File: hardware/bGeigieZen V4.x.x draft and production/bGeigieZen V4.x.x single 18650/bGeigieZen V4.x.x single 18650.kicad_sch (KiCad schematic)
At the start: 8 parts, among them J1 M5 2x15 pin, J2 Geiger IRover, J3 GPS, J4 Geiger Safepulse, J5 Extra support header

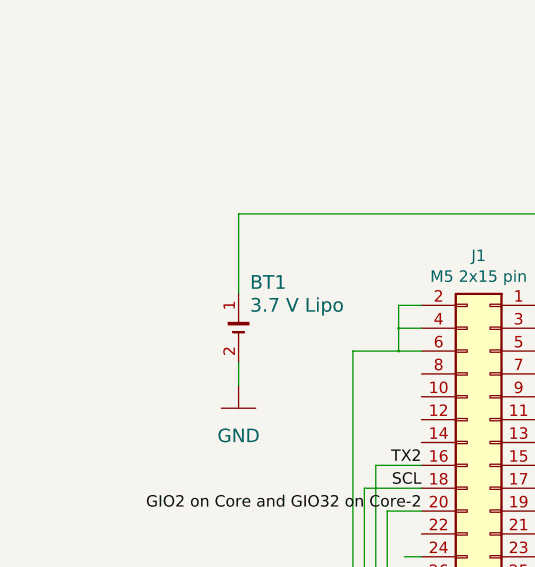
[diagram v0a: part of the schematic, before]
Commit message: reverses axp192 power setup (mistake)
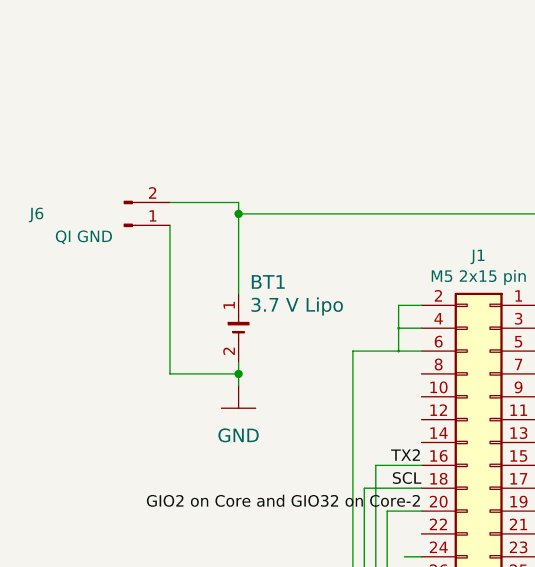
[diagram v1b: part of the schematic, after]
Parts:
- added J6: QI GND, Connector_JST:JST_PH_B2B-PH-K_1x02_P2.00mm_Vertical, symbol Connector:Conn_01x02_Male
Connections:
- net BAT: now also J6.2 (Pin_2)
- net GND: now also J6.1 (Pin_1)
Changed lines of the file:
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@@
+	)
+	(junction
+		(at 113.03 83.82)
+		(diameter 0)
+		(color 0 0 0 0)
 	)
 	(junction
@@
 	)
 	(junction
+		(at 113.03 66.04)
+		(diameter 0)
+		(color 0 0 0 0)
+	)
+	(junction
 		(at 187.96 68.58)
 		(diameter 0.3048)
@@
 	(wire
 		(pts
+			(xy 105.41 67.31) (xy 105.41 83.82)
+		)
+		(stroke
+			(width 0)
+			(type default)
+		)
+	)
+	(wire
+		(pts
 			(xy 113.03 66.04) (xy 151.765 66.04)
 		)
@@
 	(wire
 		(pts
+			(xy 105.41 83.82) (xy 113.03 83.82)
+		)
+		(stroke
+			(width 0)
+			(type default)
+		)
+	)
+	(wire
+		(pts
 			(xy 187.96 53.975) (xy 187.96 68.58)
 		)
@@
 	(wire
 		(pts
+			(xy 113.03 64.77) (xy 113.03 66.04)
+		)
+		(stroke
+			(width 0)
+			(type default)
+		)
+	)
+	(wire
+		(pts
+			(xy 113.03 83.82) (xy 113.03 85.09)
+		)
+		(stroke
+			(width 0)
+			(type default)
+		)
+	)
+	(wire
+		(pts
 			(xy 172.72 82.55) (xy 172.72 125.73)
 		)
@@
 	(wire
 		(pts
-			(xy 113.03 82.55) (xy 113.03 85.09)
+			(xy 113.03 82.55) (xy 113.03 83.82)
 		)
 		(stroke
@@
 			(width 0)
 			(type solid)
+		)
+	)
+	(wire
+		(pts
+			(xy 105.41 64.77) (xy 113.03 64.77)
+		)
+		(stroke
+			(width 0)
+			(type default)
 		)
 	)
@@
 					(unit 1)
 				)
+			)
+		)
+	)
+	(symbol
+		(lib_id "Connector:Conn_01x02_Male")
+		(at 100.33 67.31 0)
+		(mirror x)
+		(unit 1)
+		(exclude_from_sim no)
+		(in_bom yes)
+		(on_board yes)
+		(dnp no)
+		(property "Reference" "J6"
+			(at 91.44 66.04 0)
+			(effects
+				(font
+					(size 1.27 1.27)
+				)
+				(justify right)
+			)
+		)
+		(property "Value" "QI GND"
+			(at 99.06 68.58 0)
+			(effects
+				(font
+					(size 1.27 1.27)
+				)
+				(justify right)
+			)
+		)
+		(property "Footprint" "Connector_JST:JST_PH_B2B-PH-K_1x02_P2.00mm_Vertical"
+			(at 100.33 67.31 0)
+			(effects
+				(font
+					(size 1.27 1.27)
+				)
+				(hide yes)
+			)
+		)
+		(property "Datasheet" "~"
+			(at 100.33 67.31 0)
+			(effects
+				(font
+					(size 1.27 1.27)
+				)
+				(hide yes)
+			)
+		)
+		(property "Description" ""
+			(at 100.33 67.31 0)
+			(effects
+				(font
+					(size 1.27 1.27)
+				)
+				(hide yes)
+			)
+		)
+		(pin "1"
+		)
+		(pin "2"
+		)
+		(instances
+			(project "bGeigieZen V4.x.x single 18650"
+				(path "/c2e3a215-6a49-419d-95d1-595f35b17280"
+					(reference "J6")
+					(unit 1)
+				)

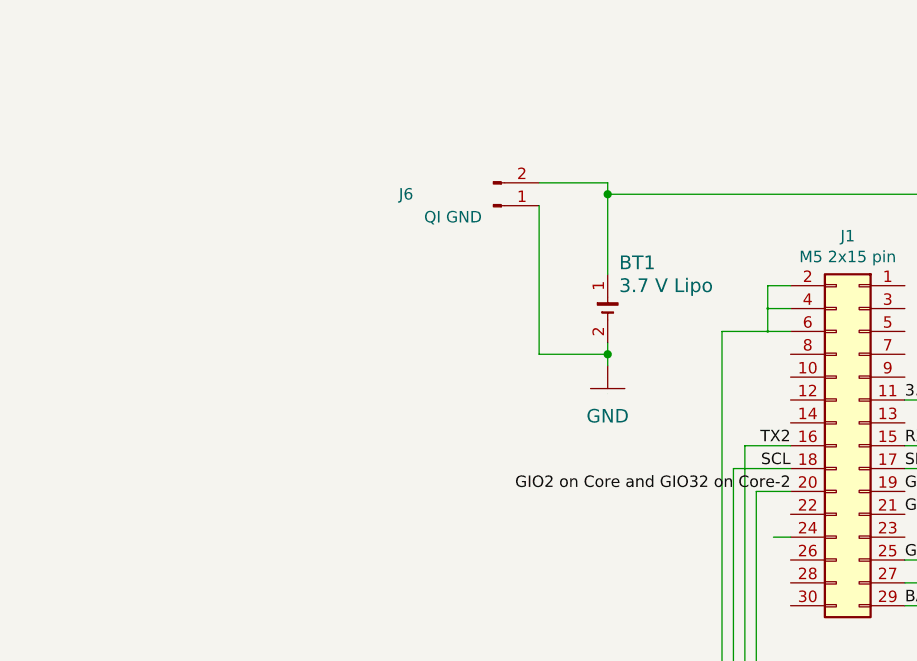
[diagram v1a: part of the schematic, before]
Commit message: Added grid and V4.0.5 boards
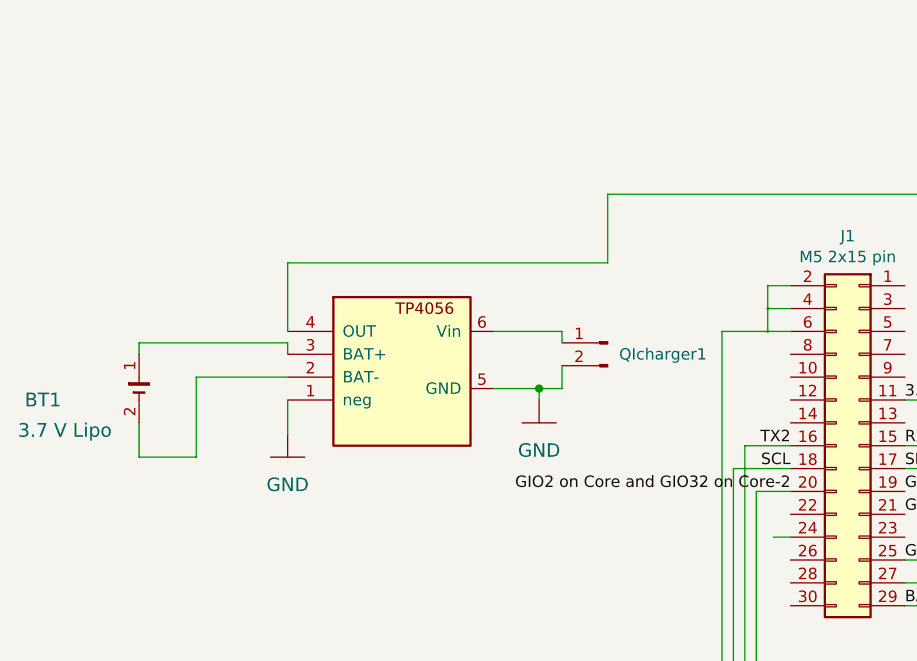
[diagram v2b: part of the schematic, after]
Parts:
- added TP4056: TP4056, bGeigieZen:TP4056, symbol tp4057:4057
- renumbered J6 to QIcharger1
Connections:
- net BAT: now also TP4056.4 (OUT); no longer BT1.1 (+), QIcharger1.2 (Pin_2)
- net GND: now also QIcharger1.2 (Pin_2), TP4056.1 (neg), TP4056.5 (GND); no longer BT1.2 (-), QIcharger1.1 (Pin_1)
- new net: BT1.1 (+), TP4056.3 (BAT+)
- new net: BT1.2 (-), TP4056.2 (BAT-)
- new net: QIcharger1.1 (Pin_1), TP4056.6 (Vin)
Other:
- moved on the sheet: BT1, QIcharger1

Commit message: Modified V4.0.5 board graphics
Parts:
- added SW1: SW_SPDT, bGeigieRaku_M5_1015:EG1206, symbol Switch:SW_SPDT
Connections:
- net BAT: now also SW1.1 (A); no longer TP4056.4 (OUT)
- new net: SW1.2 (B), TP4056.4 (OUT)
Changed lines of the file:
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@@
 	(wire
 		(pts
-			(xy 113.03 66.04) (xy 151.765 66.04)
+			(xy 113.03 66.04) (xy 115.57 66.04)
 		)
 		(stroke
@@
 	(wire
 		(pts
-			(xy 151.765 66.04) (xy 151.765 111.76)
-		)
-		(stroke
-			(width 0)
-			(type solid)
-		)
-	)
-	(wire
-		(pts
 			(xy 130.81 76.2) (xy 133.35 76.2)
 		)
@@
 	(wire
 		(pts
+			(xy 151.765 63.5) (xy 151.765 111.76)
+		)
+		(stroke
+			(width 0)
+			(type default)
+		)
+	)
+	(wire
+		(pts
 			(xy 60.96 95.25) (xy 60.96 91.44)
+		)
+		(stroke
+			(width 0)
+			(type default)
+		)
+	)
+	(wire
+		(pts
+			(xy 125.73 63.5) (xy 151.765 63.5)
 		)
 		(stroke
@@
 					(unit 1)
 				)
+			)
+		)
+	)
+	(symbol
+		(lib_id "Switch:SW_SPDT")
+		(at 120.65 66.04 0)
+		(unit 1)
+		(exclude_from_sim no)
+		(in_bom yes)
+		(on_board yes)
+		(dnp no)
+		(property "Reference" "SW1"
+			(at 120.65 58.801 0)
+			(effects
+				(font
+					(size 1.27 1.27)
+				)
+			)
+		)
+		(property "Value" "SW_SPDT"
+			(at 120.65 61.1124 0)
+			(effects
+				(font
+					(size 1.27 1.27)
+				)
+			)
+		)
+		(property "Footprint" "bGeigieRaku_M5_1015:EG1206"
+			(at 120.65 66.04 0)
+			(effects
+				(font
+					(size 1.27 1.27)
+				)
+				(hide yes)
+			)
+		)
+		(property "Datasheet" "https://www.digikey.jp/product-detail/ja/e-switch/EG1206/EG1916-ND/251333"
+			(at 120.65 66.04 0)
+			(effects
+				(font
+					(size 1.27 1.27)
+				)
+				(hide yes)
+			)
+		)
+		(property "Description" ""
+			(at 120.65 66.04 0)
+			(effects
+				(font
+					(size 1.27 1.27)
+				)
+				(hide yes)
+			)
+		)
+		(pin "1"
+		)
+		(pin "2"
+		)
+		(pin "3"
+		)
+		(instances
+			(project "bGeigieZen V4.x.x single 18650"
+				(path "/c2e3a215-6a49-419d-95d1-595f35b17280"
+					(reference "SW1")
+					(unit 1)
+				)
